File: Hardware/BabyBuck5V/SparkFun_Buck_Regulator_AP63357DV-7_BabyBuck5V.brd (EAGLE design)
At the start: 15.9 x 13.2 mm, 32 parts, among them U1 AP63357

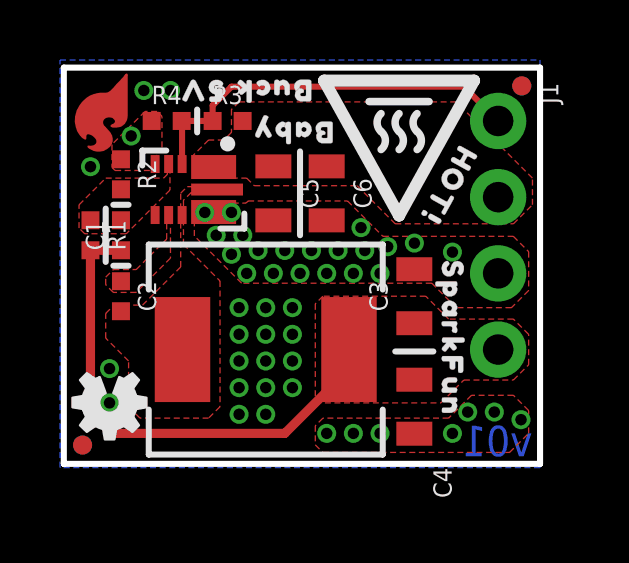
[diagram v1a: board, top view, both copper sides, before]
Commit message: Ready for v10 reds.
1x1 - Thicken silk border on U1
micro - Move fiducial to increase heat sink size
both - panelize
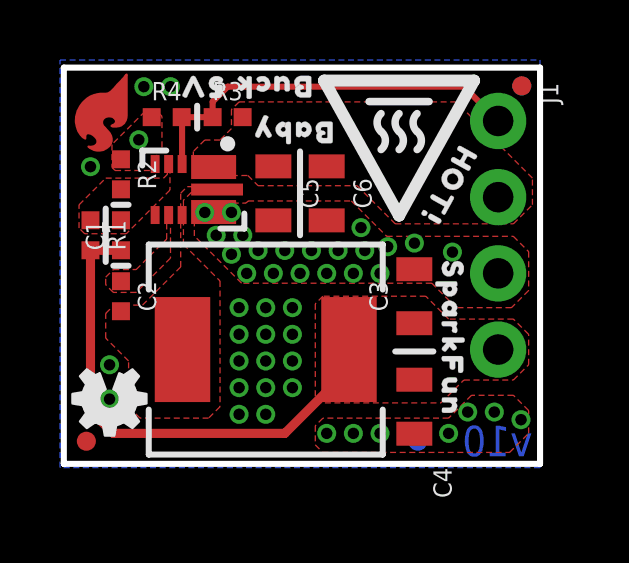
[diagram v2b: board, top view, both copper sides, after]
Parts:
- moved FD4 11.2 mm to (11.8, 0.75)
- moved FD2 0.18 mm to (0.75, 0.75)
- moved R3 0.13 mm to (5.46, 11.6)
- moved R4 0.13 mm to (3.43, 11.6)
- moved U$7 0.13 mm to (6.99, 12.6)
- moved U$9 0.13 mm to (4.57, 12.6)
- moved LOGO2 0.13 mm to (1.52, 2.16)
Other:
- board text added: "v10"
- board text removed: "v01"

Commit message: Prepare for v10 reds order.
Change R1/R2 to better match 5V output requirement.
Repanelize.
Reorganize Production Folder Structure.
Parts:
- R1: value 150k -> 220K
- R2: value 28.7k -> 41.2K
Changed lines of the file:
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@@
 <element name="LOGO2" library="SparkFun-Aesthetics" package="OSHW-LOGO-MINI" value="OSHW-LOGOMINI" x="1.524" y="2.159" smashed="yes" rot="R180"/>
 <element name="LOGO1" library="SparkFun-Aesthetics" package="BLANK" value="SFE_LOGO_NAME_FLAMEBLANK" x="14.859" y="0.254" smashed="yes"/>
-<element name="R1" library="SparkFun-Resistors" package="0402-TIGHT" value="150k" x="0.889" y="7.62" smashed="yes" rot="R270">
+<element name="R1" library="SparkFun-Resistors" package="0402-TIGHT" value="220K" x="0.889" y="7.62" smashed="yes" rot="R270">
 <attribute name="NAME" x="1.451" y="7.62" size="0.6096" layer="25" font="vector" ratio="20" rot="R270" align="bottom-center"/>
-<attribute name="PROD_ID" value="RES-15093" x="-16.891" y="-36.83" size="1.778" layer="27" rot="R270" display="off"/>
-<attribute name="RES" value="150k" x="-16.891" y="-36.83" size="1.778" layer="27" rot="R270" display="off"/>
+<attribute name="PROD_ID" value="RES-15094" x="-16.891" y="-36.83" size="1.778" layer="27" rot="R270" display="off"/>
+<attribute name="RES" value="220K" x="-16.891" y="-36.83" size="1.778" layer="27" rot="R270" display="off"/>
 <attribute name="VALUE" x="0.327" y="7.62" size="0.6096" layer="27" font="vector" ratio="20" rot="R270" align="top-center"/>
 </element>
-<element name="R2" library="Buck5V" package="0402-TIGHT" value="28.7k" x="1.905" y="9.652" smashed="yes" rot="R270">
+<element name="R2" library="Buck5V" package="0402-TIGHT" value="41.2K" x="1.905" y="9.652" smashed="yes" rot="R270">
 <attribute name="NAME" x="2.467" y="9.652" size="0.6096" layer="25" font="vector" ratio="20" rot="R270" align="bottom-center"/>
-<attribute name="PN" value="RT0402FRE0728K7L" x="1.905" y="9.652" size="1.778" layer="27" rot="R270" display="off"/>
-<attribute name="PROD_ID" value="RES-17225" x="-15.875" y="-24.638" size="1.778" layer="27" rot="R270" display="off"/>
-<attribute name="VALUE" x="1.343" y="9.652" size="0.6096" layer="27" font="vector" ratio="20" rot="R270" align="top-center"/>
+<attribute name="PN" value="RC0402FR-0741K2L" x="1.905" y="9.652" size="1.778" layer="27" rot="R270" display="off"/>
+<attribute name="PROD_ID" value="RES-15010" x="-15.875" y="-24.638" size="1.778" layer="27" rot="R270" display="off"/>
+<attribute name="VALUE" value="41.2K" x="1.343" y="9.652" size="0.6096" layer="27" font="vector" ratio="20" rot="R270" align="top-center"/>
 </element>
 <element name="R3" library="Buck5V" package="0402-TIGHT" value="93.1k" x="5.461" y="11.557" smashed="yes">

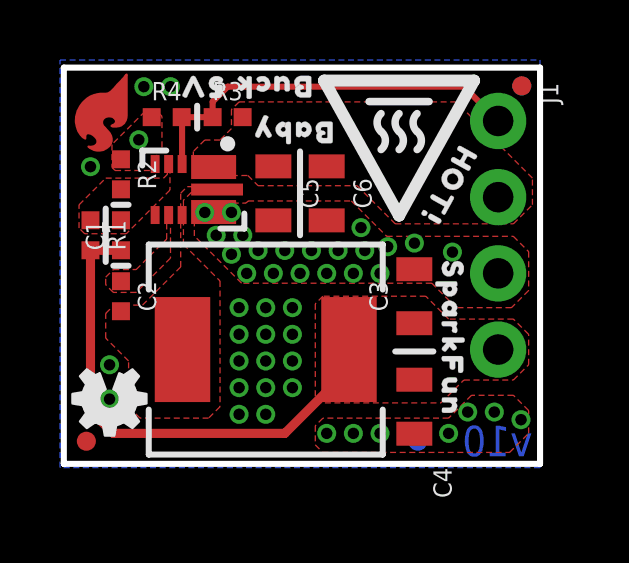
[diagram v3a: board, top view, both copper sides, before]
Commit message: Reduce paste layer on buck. Repanelize.
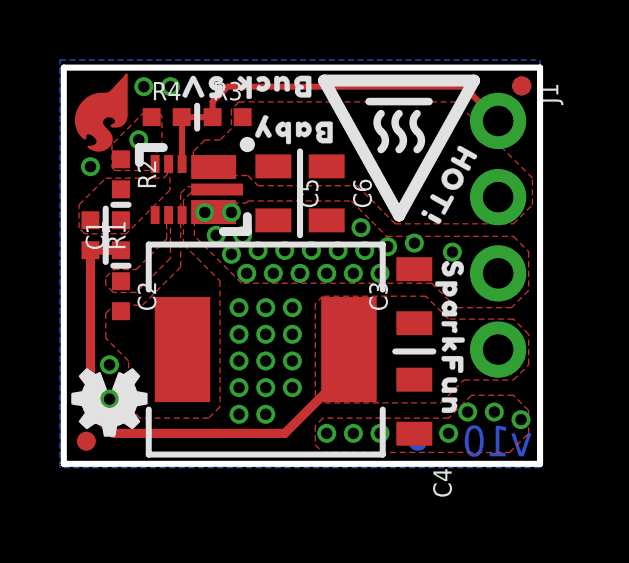
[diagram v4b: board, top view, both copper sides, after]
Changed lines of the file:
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@@
 <layer number="29" name="tStop" color="7" fill="3" visible="yes" active="yes"/>
 <layer number="30" name="bStop" color="7" fill="6" visible="yes" active="yes"/>
-<layer number="31" name="tCream" color="7" fill="4" visible="no" active="yes"/>
+<layer number="31" name="tCream" color="7" fill="4" visible="yes" active="yes"/>
 <layer number="32" name="bCream" color="7" fill="5" visible="no" active="yes"/>
 <layer number="33" name="tFinish" color="6" fill="3" visible="no" active="yes"/>
